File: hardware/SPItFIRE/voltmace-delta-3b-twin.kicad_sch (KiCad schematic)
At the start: 11 parts

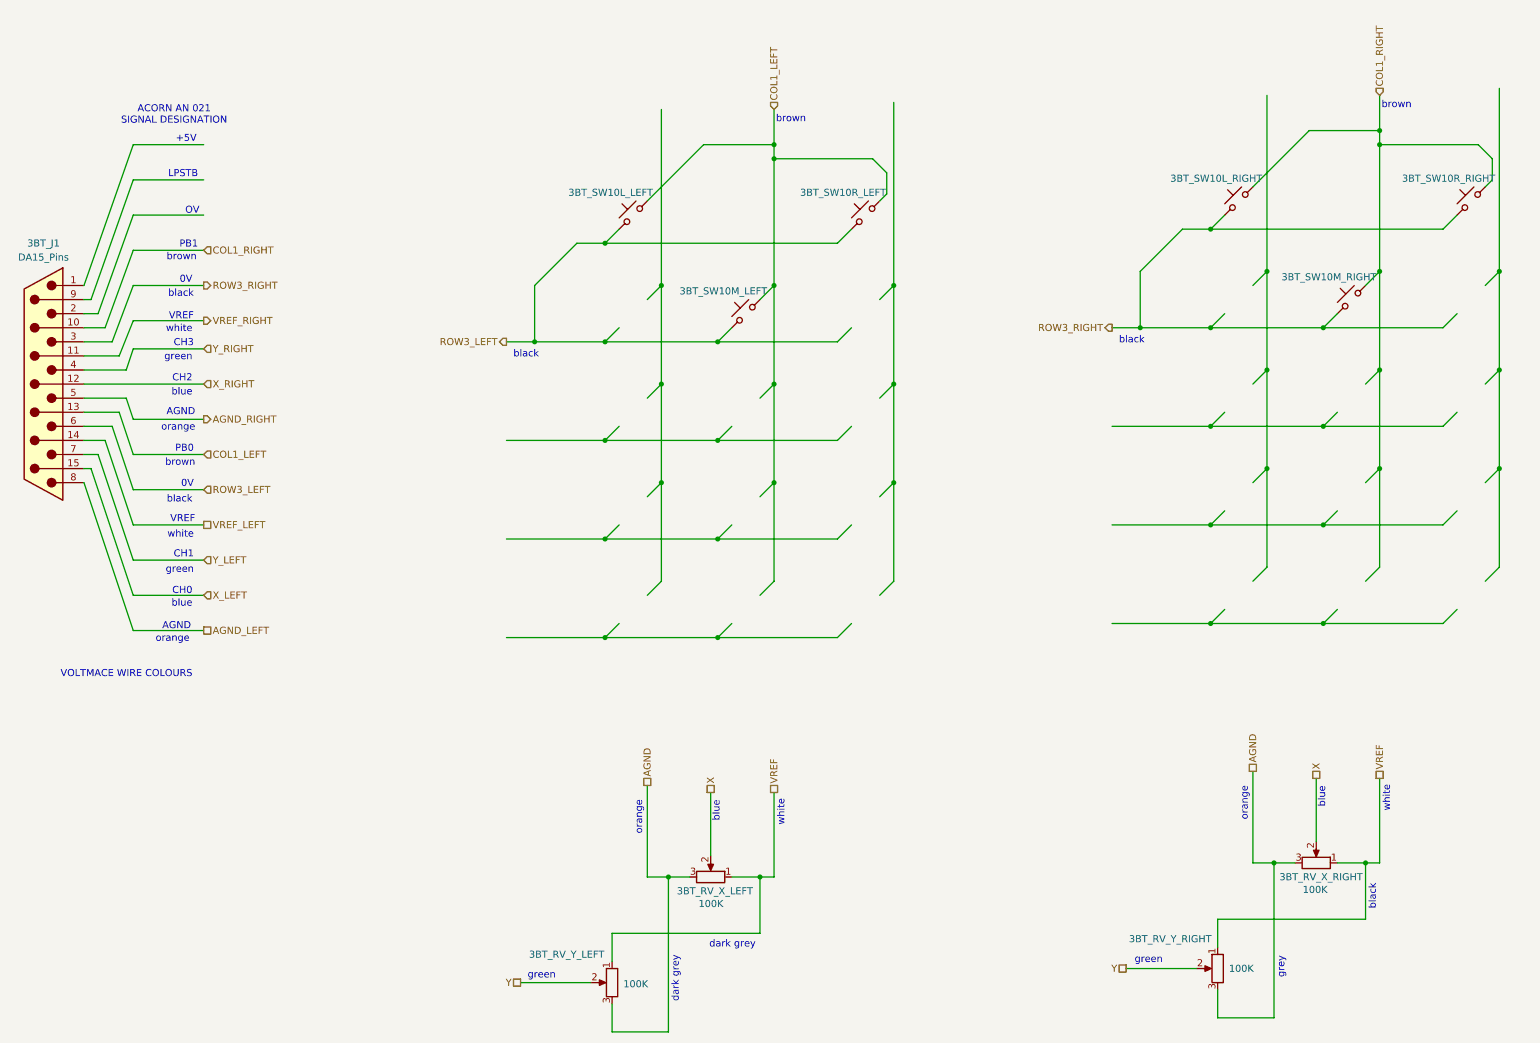
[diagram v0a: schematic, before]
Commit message: Update schematic naming convention to keep Kicad happy
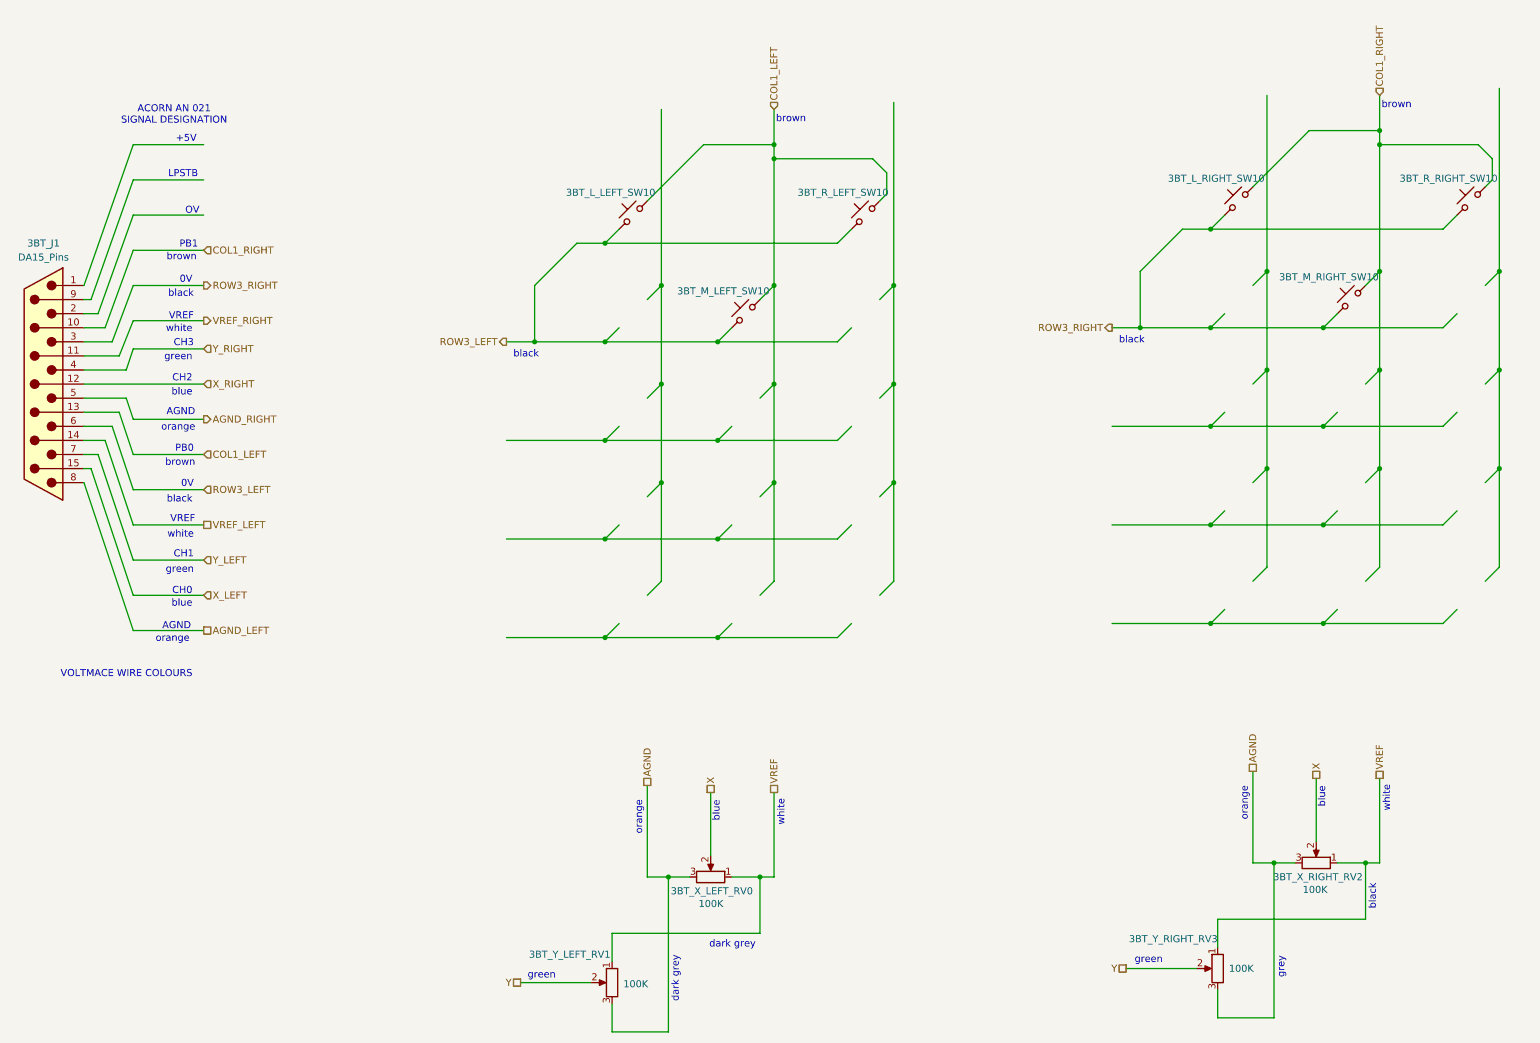
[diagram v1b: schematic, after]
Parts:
- renumbered 3BT_SW10L_LEFT to 3BT_L_LEFT_SW10, 3BT_SW10L_RIGHT to 3BT_L_RIGHT_SW10, 3BT_SW10M_LEFT to 3BT_M_LEFT_SW10, 3BT_SW10M_RIGHT to 3BT_M_RIGHT_SW10, 3BT_SW10R_LEFT to 3BT_R_LEFT_SW10, 3BT_SW10R_RIGHT to 3BT_R_RIGHT_SW10, 3BT_RV_X_LEFT to 3BT_X_LEFT_RV0, 3BT_RV_X_RIGHT to 3BT_X_RIGHT_RV2, 3BT_RV_Y_LEFT to 3BT_Y_LEFT_RV1, 3BT_RV_Y_RIGHT to 3BT_Y_RIGHT_RV3
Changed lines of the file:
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@@
 		(on_board yes)
 		(dnp no)
-		(property "Reference" "3BT_RV_X_RIGHT"
+		(property "Reference" "3BT_X_RIGHT_RV2"
 			(at 315.722 186.69 90)
 			(effects
@@
 				(path "/148e0ceb-efca-48fe-9d35-9803ba402dc8/845d2646-4b7e-4131-baf5-32413a5be084"
 					(reference "3BT_RV_X_RIGHT")
+					(unit 1)
+				)
+			)
+			(project "voltmace-delta-3b-twin"
+				(path "/4ea90652-27d3-4184-bddd-d63035d2fbfb"
+					(reference "3BT_X_RIGHT_RV2")
 					(unit 1)
 				)
@@
 		(on_board yes)
 		(dnp no)
-		(property "Reference" "3BT_SW10M_LEFT"
+		(property "Reference" "3BT_M_LEFT_SW10"
 			(at 200.406 81.026 0)
 			(effects
@@
 				(path "/148e0ceb-efca-48fe-9d35-9803ba402dc8/845d2646-4b7e-4131-baf5-32413a5be084"
 					(reference "3BT_SW10M_LEFT")
+					(unit 1)
+				)
+			)
+			(project "voltmace-delta-3b-twin"
+				(path "/4ea90652-27d3-4184-bddd-d63035d2fbfb"
+					(reference "3BT_M_LEFT_SW10")
 					(unit 1)
 				)
@@
 		(on_board yes)
 		(dnp no)
-		(property "Reference" "3BT_SW10L_RIGHT"
+		(property "Reference" "3BT_L_RIGHT_SW10"
 			(at 289.306 60.706 0)
 			(effects
@@
 				(path "/148e0ceb-efca-48fe-9d35-9803ba402dc8/845d2646-4b7e-4131-baf5-32413a5be084"
 					(reference "3BT_SW10L_RIGHT")
+					(unit 1)
+				)
+			)
+			(project "voltmace-delta-3b-twin"
+				(path "/4ea90652-27d3-4184-bddd-d63035d2fbfb"
+					(reference "3BT_L_RIGHT_SW10")
 					(unit 1)
 				)
@@
 		(on_board yes)
 		(dnp no)
-		(property "Reference" "3BT_RV_Y_LEFT"
+		(property "Reference" "3BT_Y_LEFT_RV1"
 			(at 165.354 200.66 0)
 			(effects
@@
 				(path "/148e0ceb-efca-48fe-9d35-9803ba402dc8/845d2646-4b7e-4131-baf5-32413a5be084"
 					(reference "3BT_RV_Y_LEFT")
+					(unit 1)
+				)
+			)
+			(project "voltmace-delta-3b-twin"
+				(path "/4ea90652-27d3-4184-bddd-d63035d2fbfb"
+					(reference "3BT_Y_LEFT_RV1")
 					(unit 1)
 				)
@@
 		(on_board yes)
 		(dnp no)
-		(property "Reference" "3BT_SW10M_RIGHT"
+		(property "Reference" "3BT_M_RIGHT_SW10"
 			(at 309.626 78.486 0)
 			(effects
@@
 				(path "/148e0ceb-efca-48fe-9d35-9803ba402dc8/845d2646-4b7e-4131-baf5-32413a5be084"
 					(reference "3BT_SW10M_RIGHT")
+					(unit 1)
+				)
+			)
+			(project "voltmace-delta-3b-twin"
+				(path "/4ea90652-27d3-4184-bddd-d63035d2fbfb"
+					(reference "3BT_M_RIGHT_SW10")
 					(unit 1)
 				)
@@
 		(on_board yes)
 		(dnp no)
-		(property "Reference" "3BT_RV_Y_RIGHT"
+		(property "Reference" "3BT_Y_RIGHT_RV3"
 			(at 273.558 197.866 0)
 			(effects
@@
 				(path "/148e0ceb-efca-48fe-9d35-9803ba402dc8/845d2646-4b7e-4131-baf5-32413a5be084"
 					(reference "3BT_RV_Y_RIGHT")
+					(unit 1)
+				)
+			)
+			(project "voltmace-delta-3b-twin"
+				(path "/4ea90652-27d3-4184-bddd-d63035d2fbfb"
+					(reference "3BT_Y_RIGHT_RV3")
 					(unit 1)
 				)
@@
 		(on_board yes)
 		(dnp no)
-		(property "Reference" "3BT_RV_X_LEFT"
+		(property "Reference" "3BT_X_LEFT_RV0"
 			(at 205.74 189.23 90)
 			(effects
@@
 				(path "/148e0ceb-efca-48fe-9d35-9803ba402dc8/845d2646-4b7e-4131-baf5-32413a5be084"
 					(reference "3BT_RV_X_LEFT")
+					(unit 1)
+				)
+			)
+			(project "voltmace-delta-3b-twin"
+				(path "/4ea90652-27d3-4184-bddd-d63035d2fbfb"
+					(reference "3BT_X_LEFT_RV0")
 					(unit 1)
 				)
@@
 				)
 			)
+			(project "voltmace-delta-3b-twin"
+				(path "/4ea90652-27d3-4184-bddd-d63035d2fbfb"
+					(reference "3BT_J1")
+					(unit 1)
+				)
+			)
 		)
 	)
@@
 		(on_board yes)
 		(dnp no)
-		(property "Reference" "3BT_SW10R_RIGHT"
+		(property "Reference" "3BT_R_RIGHT_SW10"
 			(at 331.216 60.706 0)
 			(effects
@@
 				(path "/148e0ceb-efca-48fe-9d35-9803ba402dc8/845d2646-4b7e-4131-baf5-32413a5be084"
 					(reference "3BT_SW10R_RIGHT")
+					(unit 1)
+				)
+			)
+			(project "voltmace-delta-3b-twin"
+				(path "/4ea90652-27d3-4184-bddd-d63035d2fbfb"
+					(reference "3BT_R_RIGHT_SW10")
 					(unit 1)
 				)
@@
 		(on_board yes)
 		(dnp no)
-		(property "Reference" "3BT_SW10R_LEFT"
+		(property "Reference" "3BT_R_LEFT_SW10"
 			(at 221.996 63.246 0)
 			(effects
@@
 				(path "/148e0ceb-efca-48fe-9d35-9803ba402dc8/845d2646-4b7e-4131-baf5-32413a5be084"
 					(reference "3BT_SW10R_LEFT")
+					(unit 1)
+				)
+			)
+			(project "voltmace-delta-3b-twin"
+				(path "/4ea90652-27d3-4184-bddd-d63035d2fbfb"
+					(reference "3BT_R_LEFT_SW10")
 					(unit 1)
 				)
@@
 		(on_board yes)
 		(dnp no)
-		(property "Reference" "3BT_SW10L_LEFT"
+		(property "Reference" "3BT_L_LEFT_SW10"
 			(at 180.086 63.246 0)
 			(effects
@@
 				)
 			)
-		)
-	)
+			(project "voltmace-delta-3b-twin"
+				(path "/4ea90652-27d3-4184-bddd-d63035d2fbfb"
+					(reference "3BT_L_LEFT_SW10")
+					(unit 1)
+				)
+			)
+		)
+	)
+	(sheet_instances
+		(path "/"
+			(page "1")
+		)
+	)
+	(embedded_fonts no)
 )

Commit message: The bulk of the schematic layout for the board (pending review and check)
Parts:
- renumbered 3BT_X_LEFT_RV0 to 3BT_RV_X_LEFT, 3BT_X_RIGHT_RV2 to 3BT_RV_X_RIGHT, 3BT_Y_LEFT_RV1 to 3BT_RV_Y_LEFT, 3BT_Y_RIGHT_RV3 to 3BT_RV_Y_RIGHT, 3BT_L_LEFT_SW10 to 3BT_SW10L_LEFT, 3BT_L_RIGHT_SW10 to 3BT_SW10L_RIGHT, 3BT_M_LEFT_SW10 to 3BT_SW10M_LEFT, 3BT_M_RIGHT_SW10 to 3BT_SW10M_RIGHT, 3BT_R_LEFT_SW10 to 3BT_SW10R_LEFT, 3BT_R_RIGHT_SW10 to 3BT_SW10R_RIGHT

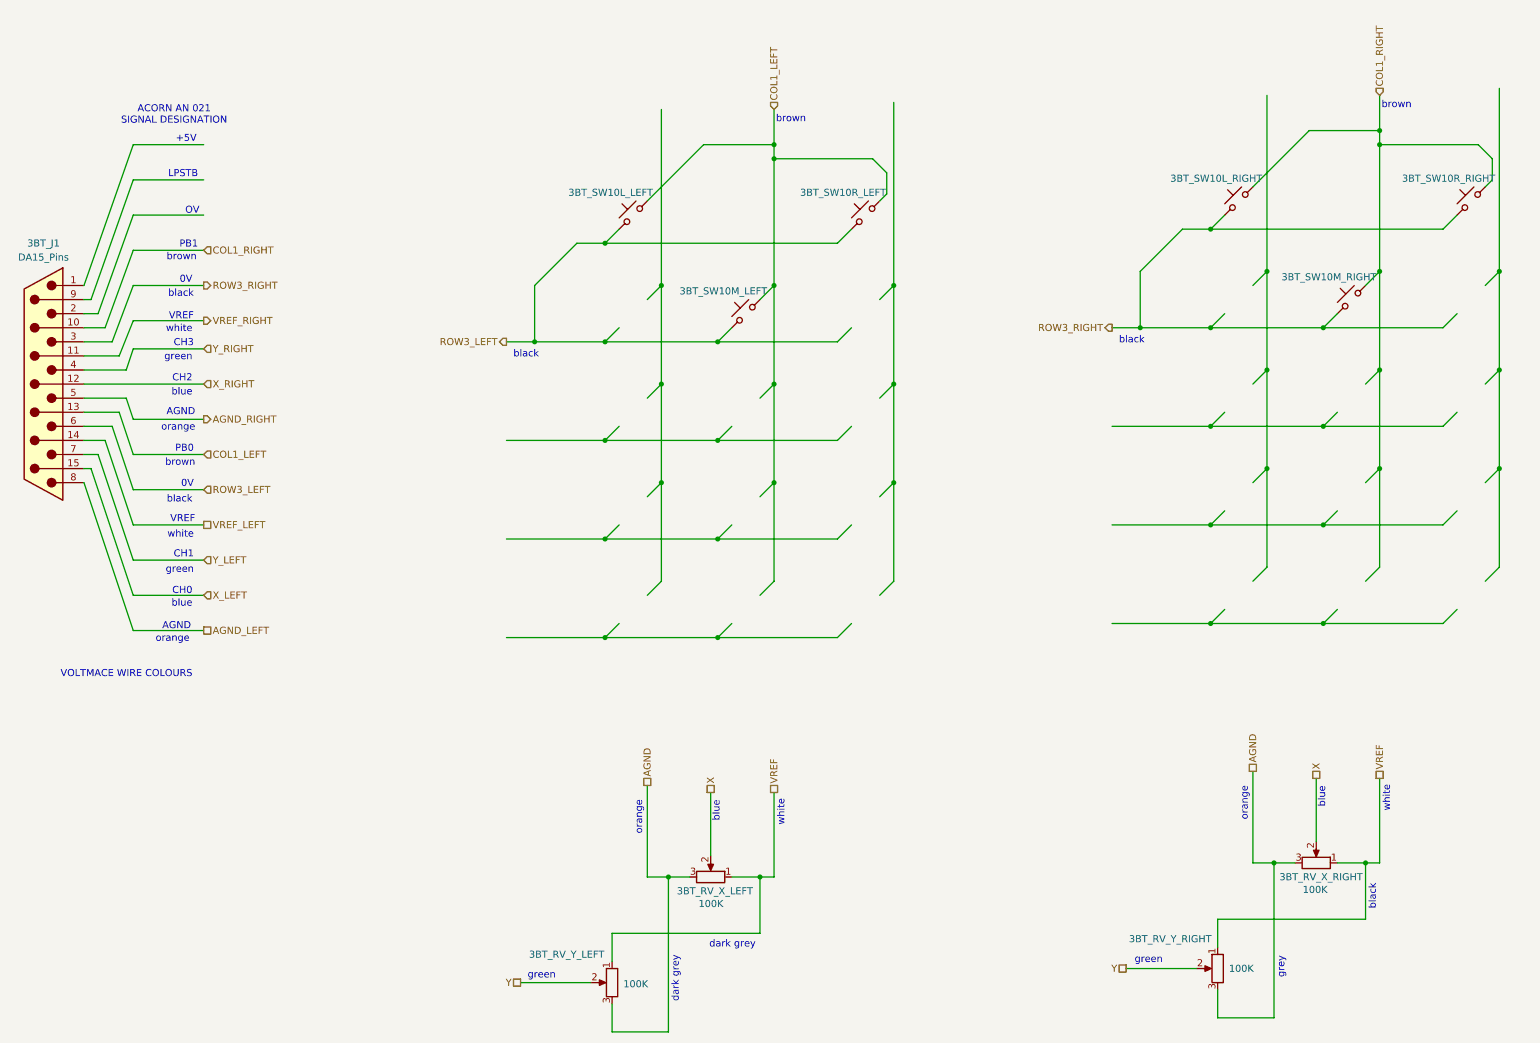
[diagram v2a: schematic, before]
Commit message: Schematic updates and rule checking
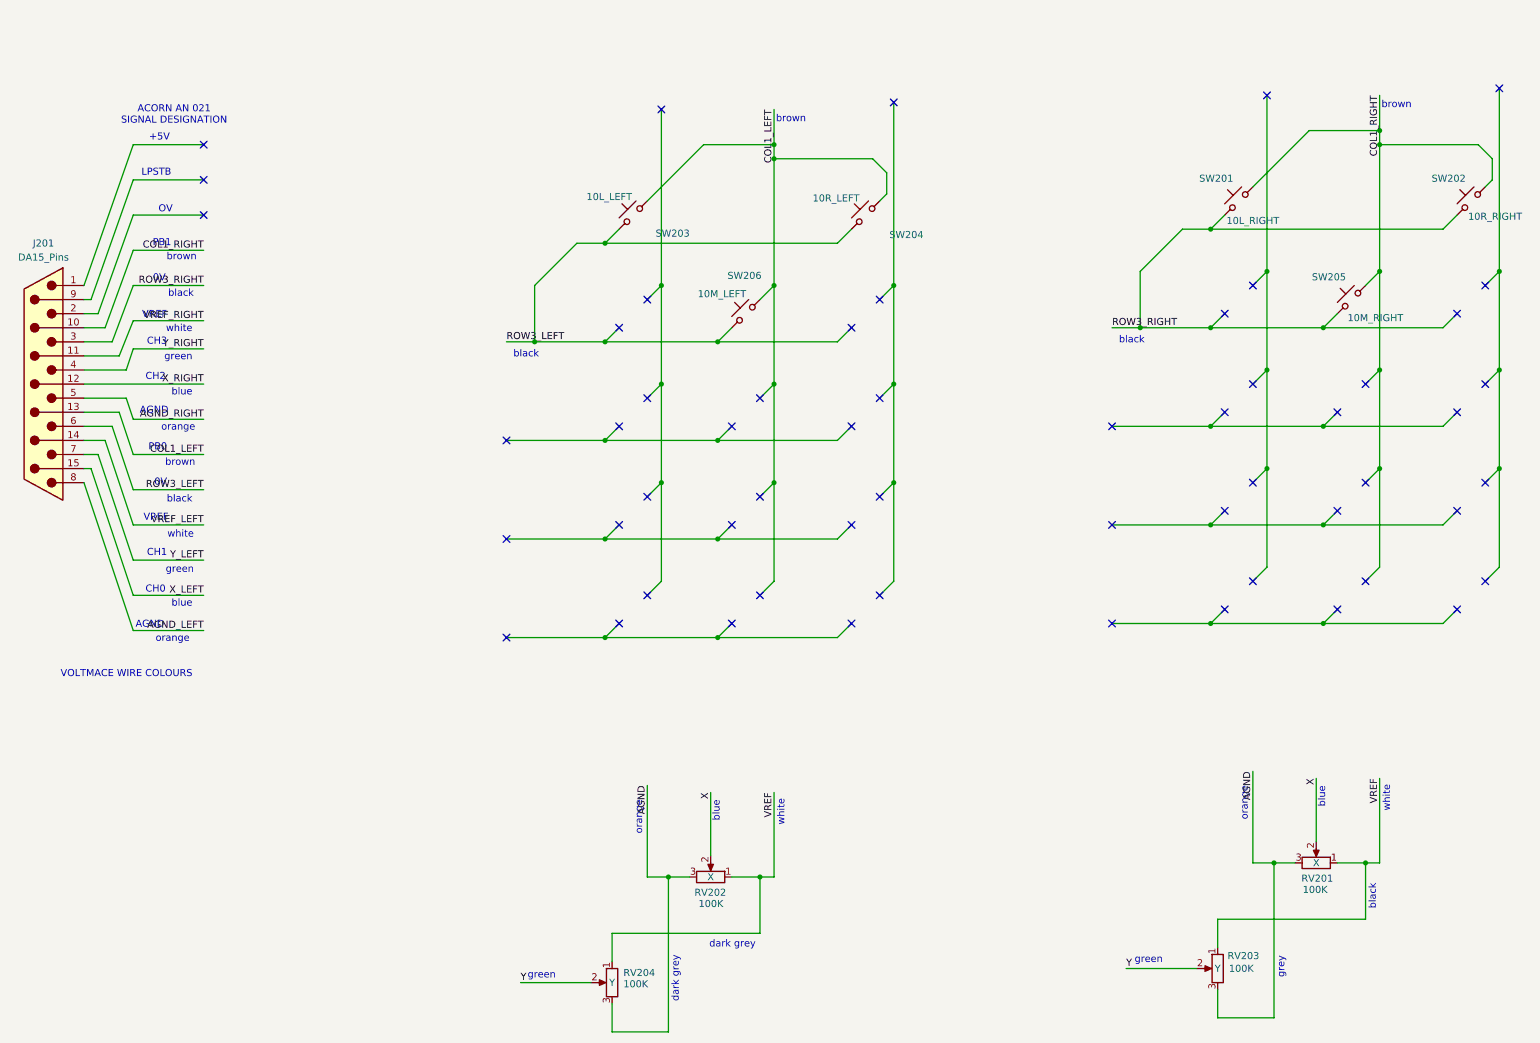
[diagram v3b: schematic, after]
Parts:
- RV201: renamed from 3BT_RV_X_RIGHT; Axis (none) -> X
- RV202: renamed from 3BT_RV_X_LEFT; Axis (none) -> X
- RV203: renamed from 3BT_RV_Y_RIGHT; Axis (none) -> Y
- RV204: renamed from 3BT_RV_Y_LEFT; Axis (none) -> Y
- SW201: renamed from 3BT_SW10L_RIGHT; value SW_Push_45deg -> 10L_RIGHT
- SW202: renamed from 3BT_SW10R_RIGHT; value SW_Push_45deg -> 10R_RIGHT
- SW203: renamed from 3BT_SW10L_LEFT; value SW_Push_45deg -> 10L_LEFT
- SW204: renamed from 3BT_SW10R_LEFT; value SW_Push_45deg -> 10R_LEFT
- SW205: renamed from 3BT_SW10M_RIGHT; value SW_Push_45deg -> 10M_RIGHT
- SW206: renamed from 3BT_SW10M_LEFT; value SW_Push_45deg -> 10M_LEFT
- renumbered 3BT_J1 to J201
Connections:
- no-connect marks 0 -> 57
